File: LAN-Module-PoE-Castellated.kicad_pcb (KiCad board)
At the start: 2 copper layers, 25.3 x 61 mm, 105 parts, among them J1 HY931147C, J10 ProtoCastellatedHeader, J11 ProtoCastellatedHeader, J12 ProtoCastellatedHeader, J13 ProtoCastellatedHeader, J14 ProtoCastellatedHeader, J15 ProtoCastellatedHeader, J16 ProtoCastellatedHeader, J17 ProtoCastellatedHeader, J18 ProtoCastellatedHeader, J19 ProtoCastellatedHeader, J2 ProtoCastellatedHeader, J20 ProtoCastellatedHeader, J21 ProtoCastellatedHeader, J22 ProtoCastellatedHeader, J23 ProtoCastellatedHeader, J24 ProtoCastellatedHeader, J25 ProtoCastellatedHeader, J26 ProtoCastellatedHeader, J27 ProtoCastellatedHeader, J28 ProtoCastellatedHeader, J29 ProtoCastellatedHeader, J3 ProtoCastellatedHeader, J4 ProtoCastellatedHeader, J5 ProtoCastellatedHeader, J6 ProtoCastellatedHeader, J7 ProtoCastellatedHeader, J8 ProtoCastellatedHeader, J9 ProtoCastellatedHeader, SW1 RESET, U1 ESP32-U4WDH, U2 Si3404, U3 LV2842XLVDDCR, U4 RTL8201F, Y1 40MHz

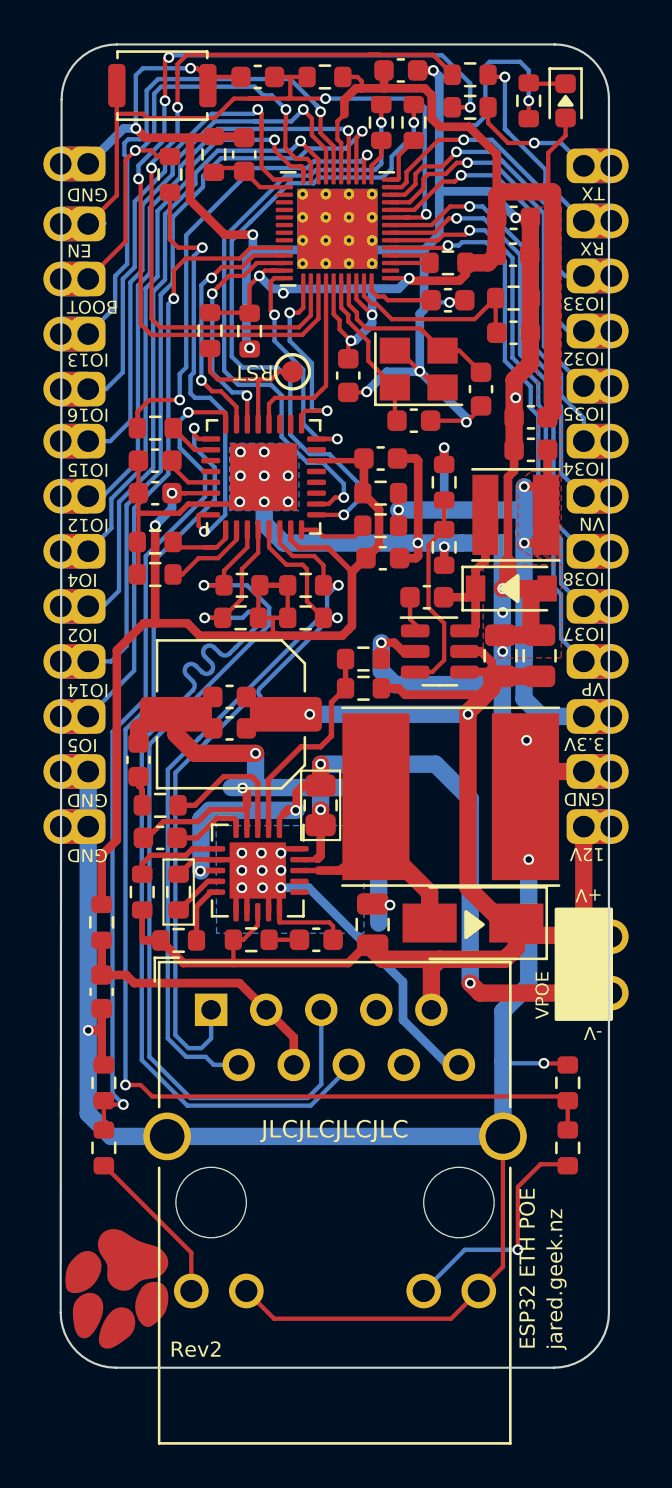
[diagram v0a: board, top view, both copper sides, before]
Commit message: HW REV: Fix stability issue
Important change required to ensure stability across different types of ethernet switches.

I had only tested this with a TP-LINK switch, but the design did not work with other switches, and the reference schematic does NOT specify that the CT/termination resistors should be tied to 3.3V. Instead they should be coupled to GND through a capacitor (of unspecified value).
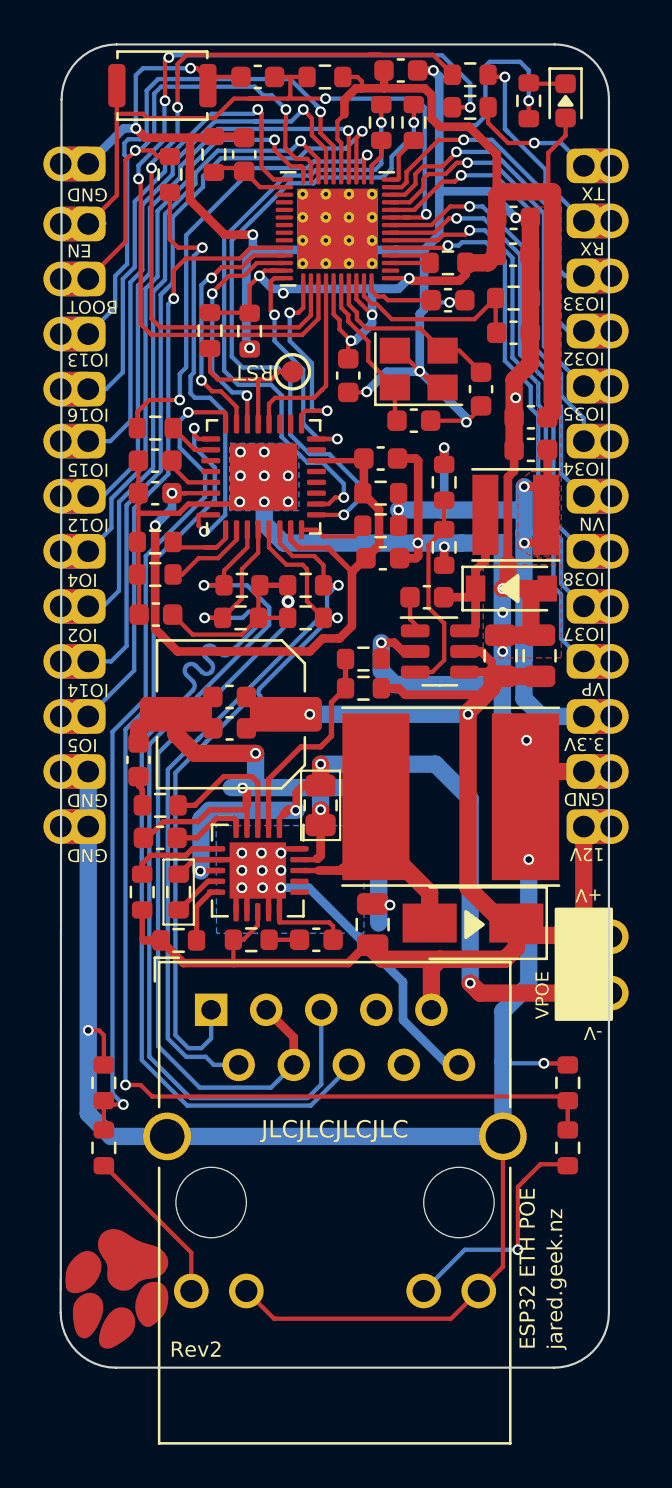
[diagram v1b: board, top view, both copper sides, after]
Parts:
- removed R25: 0R, Resistor_SMD:R_0603_1608Metric
- moved C3 17.6 mm to (33.6, 58.8), turned to 0 degrees
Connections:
- R13 pad 1: /LAN_3P3V -> /MDI0_CT
- R14 pad 1: /LAN_3P3V -> /MDI0_CT
- R17 pad 1: /LAN_3P3V -> /MDI0_CT
- R18 pad 1: /LAN_3P3V -> /MDI0_CT
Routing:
- net /MDI0_CT: track 12.9 -> 43.9 mm, vias 0 -> 1
- net /LAN_3P3V: track 53.6 -> 34.0 mm
- net GND: track 238.9 -> 236.5 mm
